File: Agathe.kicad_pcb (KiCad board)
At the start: 2 copper layers, 173 parts, among them SW1 SW_Push, U1 ATmega32U4-AU, Y1 Crystal_GND24_Small

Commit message: day 2 of work
MCU and USB routed
All switch routed between them
Todo: connect row and column to MCU
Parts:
- removed D44, D60, D62, D64, D67, D69, D71, D72: D_Small, Diode_SMD:D_SOD-123
- removed D76, D77: 3.6V, Diode_SMD:D_SOD-123
- removed MX44, MX60, MX67, MX69, MX71, MX72: MX-NoLED, MX_Only:MXOnly-1U-NoLED
- removed MX62: MX-NoLED, MX_Only:MXOnly-1.25U-NoLED
- removed MX64: MX-NoLED, MX_Only:MXOnly-2U-ReversedStabilizers-NoLED
- removed R7, R8: 75R, Resistor_SMD:R_0805_2012Metric
- removed R9: 1.5k, Resistor_SMD:R_0805_2012Metric
- added U2: PRTR5V0U2X, Package_TO_SOT_SMD:SOT-143, B.Cu at (180.2, 106.4)
- C1, C2, C3, C4, C5, C6, D10, D11, D12, D13, D14, D15, D16, D17, D18, D19, D2, D20, D21, D22, D23, D24, D25, D26, D27, D28, D29, D3, D30, D31, D32, D33, D34, D35, D36, D37, D38, D39, D4, D40, D41, D42, D43, D45, D46, D47, D48, D49, D5, D50, D51, D52, D53, D54, D55, D56, D57, D58, D59, D6, D61, D63, D65, D66, D68, D7, D70, D73, D74, D75, D8, D9, F1, R1, R2, R3, R4, R5, R6, Y1: moved to B.Cu
- C7: footprint Diode_SMD:D_SOD-123 -> Capacitor_SMD:C_0805_2012Metric; moved to B.Cu
- MX31: footprint MX_Only:MXOnly-1.25U-NoLED -> MX_Only:MXOnly-1.75U-NoLED
- MX43: footprint MX_Only:MXOnly-2.25U-NoLED -> MX_Only:MXOnly-2.25U-ReversedStabilizers-NoLED
- USB1: footprint Keebio-Parts:HRO-TYPE-C-31-M-12-Assembly -> Connector_USB:USB_C_Receptacle_HRO_TYPE-C-31-M-12
- moved D73 394.8 mm to (333.9, 181.0), turned to 90 degrees
- moved D59 381.3 mm to (353.0, 161.9), turned to 90 degrees
- moved D58 373.2 mm to (326.8, 161.9), turned to 90 degrees
- moved D45 332.8 mm to (371.7, 142.9), turned to 90 degrees
- moved D43 332.6 mm to (336.9, 142.9), turned to 90 degrees
- moved D70 328.8 mm to (262.8, 180.9), turned to 102 degrees
- moved D74 327.3 mm to (353.0, 181.0), turned to 90 degrees
- moved D75 324.1 mm to (372.0, 181.0), turned to 90 degrees
- moved D14 308.5 mm to (331.3, 104.8), turned to 90 degrees
- moved D68 299.2 mm to (225.5, 188.8), turned to 102 degrees
- moved D13 287.2 mm to (302.7, 104.8), turned to 90 degrees
- moved D30 273.7 mm to (367.6, 123.8), turned to 90 degrees
- moved D12 273.7 mm to (283.7, 104.8), turned to 90 degrees
- moved D56 270.2 mm to (281.6, 161.9), turned to 90 degrees
- moved D57 262.5 mm to (300.6, 161.9), turned to 90 degrees
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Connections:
- U1 pad 18: ROW0 -> COL13
- U1 pad 19: ROW1 -> COL12
- U1 pad 26: COL13 -> COL0
- U1 pad 27: COL12 -> COL1
- U1 pad 40: COL1 -> ROW1
- U1 pad 41: COL0 -> ROW0
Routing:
- net ROW4: track 0.00 -> 320.5 mm
- net GND: track 0.00 -> 274.8 mm, vias 0 -> 3
- net ROW0: track 0.00 -> 273.3 mm
- net ROW1: track 0.00 -> 268.1 mm
- net ROW2: track 0.00 -> 266.4 mm
- net ROW3: track 0.00 -> 257.3 mm
- net +5V: track 0.00 -> 151.3 mm, vias 0 -> 4
- net COL12: track 0.00 -> 99.8 mm
- net COL9: track 0.00 -> 87.3 mm
- net COL4: track 0.00 -> 86.8 mm
- net COL5: track 0.00 -> 86.8 mm
- net COL7: track 0.00 -> 86.0 mm
- net COL2: track 0.00 -> 85.7 mm
- net COL13: track 0.00 -> 85.2 mm
- net COL14: track 0.00 -> 81.9 mm
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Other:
- net class Default: trace_width 0.25 -> 0.254
- net class Power added: clearance 0.2, trace_width 0.381, via_dia 0.8, via_drill 0.4

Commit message: Route everything
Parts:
- moved D45 7.14 mm to (364.6, 144.0), turned to 0 degrees
- moved D75 7.14 mm to (365.0, 182.1), turned to 0 degrees
- moved SW1 3.71 mm to (194.4, 101.1)
- moved USB1 3.71 mm to (179.3, 93.1)
- moved F1 3.71 mm to (170.0, 99.8)
- moved R4 3.71 mm to (190.4, 105.8)
- moved R5 3.71 mm to (172.9, 99.5)
- moved R6 3.71 mm to (185.6, 99.5)
- moved U2 3.71 mm to (180.1, 102.7)
- moved D56 0.49 mm to (281.5, 161.4)
- moved D57 0.49 mm to (300.5, 161.4)
- moved D58 0.49 mm to (326.7, 161.4)
- moved D70 0.49 mm to (262.7, 180.4)
- moved MX40 0.49 mm to (258.2, 139.7)
- moved MX42 0.49 mm to (298.0, 139.7)
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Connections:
- U1 pad 1: COL2 -> Net-(U1-Pad1)
- U1 pad 10: Net-(U1-Pad10) -> COL9
- U1 pad 11: COL14 -> COL10
- U1 pad 12: COL9 -> COL11
- U1 pad 20: ROW2 -> ROW4
- U1 pad 22: ROW4 -> ROW2
- U1 pad 25: COL6 -> COL5
- U1 pad 26: COL0 -> COL4
- U1 pad 27: COL1 -> COL3
- U1 pad 28: COL11 -> COL2
- U1 pad 29: COL10 -> COL1
- U1 pad 30: COL5 -> COL0
- U1 pad 31: COL4 -> COL6
- U1 pad 32: COL3 -> COL14
- U1 pad 8: COL8 -> COL7
- U1 pad 9: COL7 -> COL8
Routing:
- net COL14: track 81.9 -> 334.4 mm, vias 0 -> 1
- net COL13: track 85.2 -> 303.2 mm, vias 0 -> 1
- net COL12: track 99.8 -> 291.4 mm, vias 0 -> 1
- net COL0: track 80.2 -> 256.9 mm, vias 0 -> 1
- net COL1: track 62.0 -> 219.0 mm, vias 0 -> 1
- net COL11: track 73.1 -> 220.3 mm, vias 0 -> 1
- net COL10: track 70.4 -> 207.0 mm, vias 0 -> 1
- net COL2: track 85.7 -> 218.2 mm, vias 0 -> 1
- net COL3: track 65.6 -> 177.1 mm, vias 0 -> 1
- net COL9: track 87.3 -> 186.7 mm, vias 0 -> 1
- net COL8: track 67.4 -> 162.6 mm, vias 0 -> 1
- net COL4: track 86.8 -> 178.5 mm, vias 0 -> 1
- net GND: track 274.8 -> 199.1 mm, vias 3 -> 2
- net ROW3: track 257.3 -> 332.9 mm, vias 0 -> 2
- net ROW0: track 273.3 -> 333.0 mm, vias 0 -> 4
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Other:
- board outline added: 338.8 x 114.1 mm

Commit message: change the enter footprint
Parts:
- MX43: footprint MX_Only:MXOnly-2.25U-ReversedStabilizers-NoLED -> MX_Only:MXOnly-2.25U-NoLED
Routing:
- net COL12: track 291.4 -> 293.9 mm
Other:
- board size 338.8 x 114.1 mm -> 338.8 x 114.8 mm

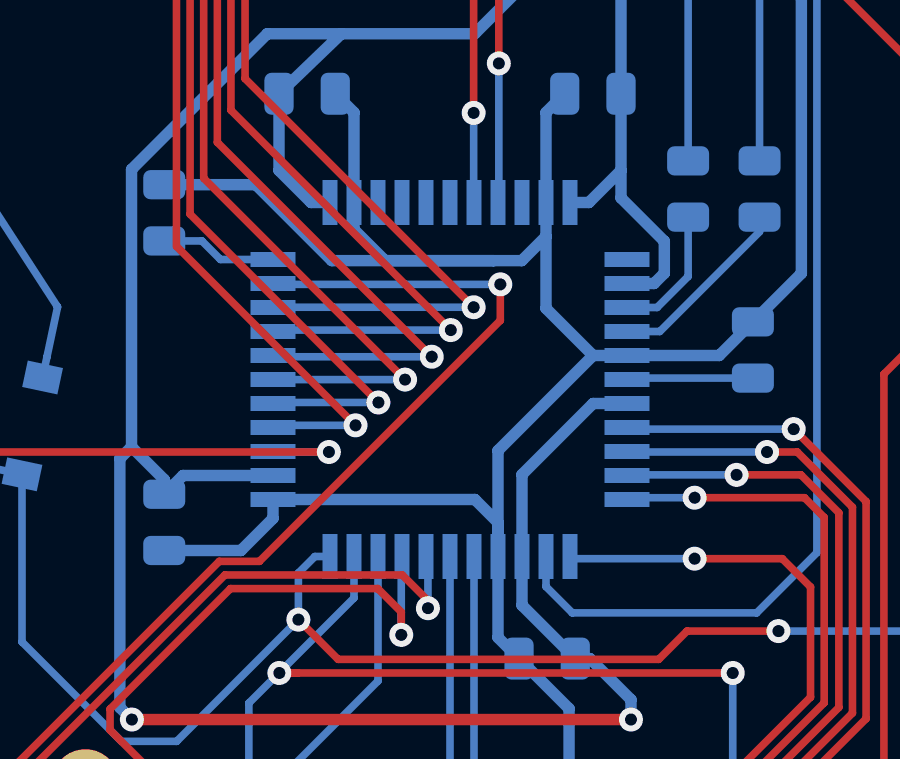
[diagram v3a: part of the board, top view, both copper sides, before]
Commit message: Add a proper usb-c
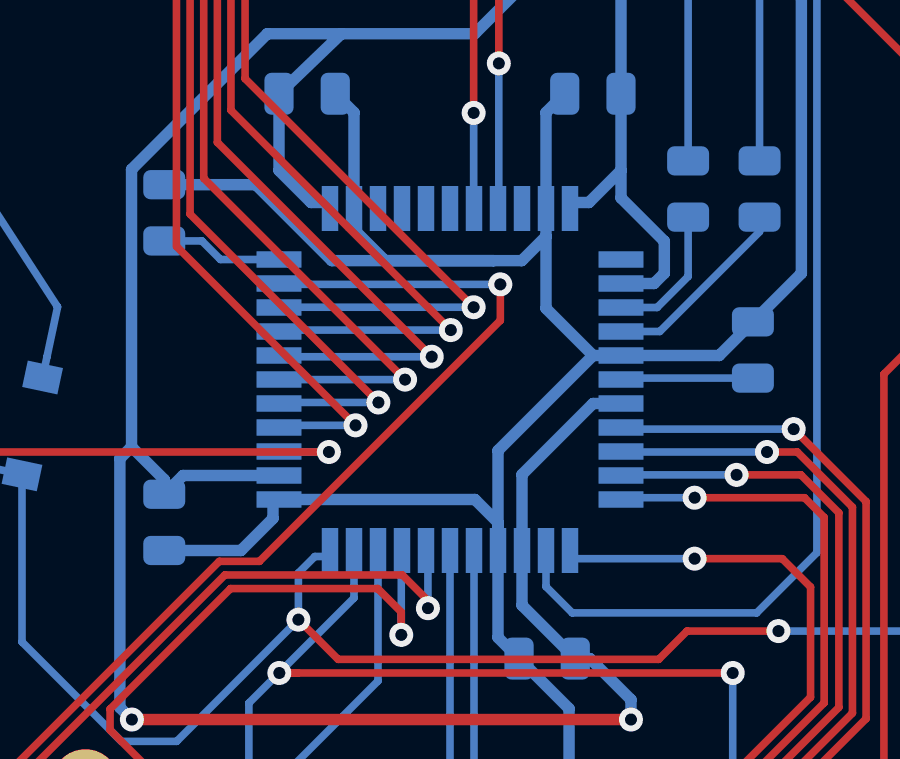
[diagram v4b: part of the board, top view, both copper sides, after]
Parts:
- U1: footprint Keebio-Parts:ATMEGA32U4-AU -> Package_QFP:TQFP-44_10x10mm_P0.8mm

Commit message: Add rotary encoder support
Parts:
- MX15, MX30, MX45: value MX-NoLED -> Rotary_Encoder_Switch; footprint MX_Only:MXOnly-1U-NoLED -> Rotary_Encoder:rotary_x_MX
- U1: footprint Package_QFP:TQFP-44_10x10mm_P0.8mm -> Keebio-Parts:ATMEGA32U4-AU
- moved D30 15.9 mm to (351.6, 123.3)
- moved D15 15.7 mm to (347.7, 104.3)
- moved D45 9.16 mm to (355.6, 142.4), turned to 90 degrees
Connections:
- U1 pad 38: Net-(U1-Pad38) -> COL7
- U1 pad 39: Net-(U1-Pad39) -> COL8
- U1 pad 8: COL7 -> ROTB
- U1 pad 9: COL8 -> ROTA
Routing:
- net ROTA: track 0.00 -> 255.0 mm, vias 0 -> 2
- net ROTB: track 0.00 -> 246.8 mm, vias 0 -> 2
- net GND: track 199.1 -> 264.9 mm
- net COL14: track 334.4 -> 380.8 mm
- net COL7: track 140.3 -> 162.7 mm
- net COL8: track 162.6 -> 181.1 mm
- net ROW1: track 317.4 -> 301.5 mm
- net ROW0: track 333.0 -> 317.3 mm
- net Net-(D45-Pad2): track 11.1 -> 19.9 mm
- net Net-(D30-Pad2): track 11.4 -> 19.8 mm
- net Net-(D15-Pad2): track 11.4 -> 19.6 mm
- net ROW2: track 319.5 -> 312.1 mm

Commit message: Add underglow
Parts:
- added LED1: WS2812B, LED_SMD:LED_WS2812B_PLCC4_5.0x5.0mm_P3.2mm, B.Cu at (193.5, 71.7)
- added LED10: WS2812B, LED_SMD:LED_WS2812B_PLCC4_5.0x5.0mm_P3.2mm, B.Cu at (302.7, 162.7)
- added LED11: WS2812B, LED_SMD:LED_WS2812B_PLCC4_5.0x5.0mm_P3.2mm, B.Cu at (362.8, 162.7)
- added LED12: WS2812B, LED_SMD:LED_WS2812B_PLCC4_5.0x5.0mm_P3.2mm, B.Cu at (375.2, 137.3)
- added LED13: WS2812B, LED_SMD:LED_WS2812B_PLCC4_5.0x5.0mm_P3.2mm, B.Cu at (375.2, 99.2)
- added LED14: WS2812B, LED_SMD:LED_WS2812B_PLCC4_5.0x5.0mm_P3.2mm, B.Cu at (347.4, 71.7)
- added LED15: WS2812B, LED_SMD:LED_WS2812B_PLCC4_5.0x5.0mm_P3.2mm, B.Cu at (290.3, 71.7)
- added LED16: WS2812B, LED_SMD:LED_WS2812B_PLCC4_5.0x5.0mm_P3.2mm, B.Cu at (235.9, 71.7)
- added LED2: WS2812B, LED_SMD:LED_WS2812B_PLCC4_5.0x5.0mm_P3.2mm, B.Cu at (139.7, 71.7)
- added LED3: WS2812B, LED_SMD:LED_WS2812B_PLCC4_5.0x5.0mm_P3.2mm, B.Cu at (70.9, 71.7)
- added LED4: WS2812B, LED_SMD:LED_WS2812B_PLCC4_5.0x5.0mm_P3.2mm, B.Cu at (43.3, 99.2)
- added LED5: WS2812B, LED_SMD:LED_WS2812B_PLCC4_5.0x5.0mm_P3.2mm, B.Cu at (43.3, 137.3)
- added LED6: WS2812B, LED_SMD:LED_WS2812B_PLCC4_5.0x5.0mm_P3.2mm, B.Cu at (76.8, 162.7)
- added LED7: WS2812B, LED_SMD:LED_WS2812B_PLCC4_5.0x5.0mm_P3.2mm, B.Cu at (139.7, 170.7)
- added LED8: WS2812B, LED_SMD:LED_WS2812B_PLCC4_5.0x5.0mm_P3.2mm, B.Cu at (188.4, 179.4)
- added LED9: WS2812B, LED_SMD:LED_WS2812B_PLCC4_5.0x5.0mm_P3.2mm, B.Cu at (242.3, 169.3)
- moved D66 23.0 mm to (178.8, 174.1)
- moved D63 23.0 mm to (118.2, 161.3)
- moved D65 23.0 mm to (148.5, 167.7)
- moved D73 23.0 mm to (338.9, 158.1)
- moved D74 23.0 mm to (357.9, 158.1)
- moved D61 23.0 mm to (62.0, 158.1)
- moved D70 23.0 mm to (267.7, 158.0)
- moved D75 23.0 mm to (370.0, 159.7)
- moved D48 22.0 mm to (119.9, 143.2)
- moved MX7 22.0 mm to (175.9, 93.9)
- moved D41 22.0 mm to (291.9, 121.0)
- moved MX36 22.0 mm to (163.3, 130.2)
- moved MX39 22.0 mm to (244.6, 122.2)
- moved D3 22.0 mm to (107.3, 82.9)
- moved D14 22.0 mm to (336.2, 82.9)
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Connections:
- U1 pad 30: COL0 -> LED
- U1 pad 31: COL6 -> COL0
- U1 pad 36: Net-(U1-Pad36) -> COL6
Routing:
- net +5V: track 158.4 -> 985.7 mm, vias 4 -> 5
- net LED: track 0.00 -> 105.2 mm, vias 0 -> 4
- net Net-(LED2-Pad2): track 0.00 -> 65.6 mm
- net Net-(LED6-Pad2): track 0.00 -> 59.3 mm
- net Net-(LED10-Pad4): track 0.00 -> 58.1 mm
- net Net-(LED10-Pad2): track 0.00 -> 57.0 mm
- net Net-(LED13-Pad2): track 0.00 -> 53.7 mm
- net Net-(LED14-Pad2): track 0.00 -> 53.6 mm
- net Net-(LED8-Pad2): track 0.00 -> 52.5 mm
- net Net-(LED1-Pad2): track 0.00 -> 51.3 mm
- net Net-(LED15-Pad2): track 0.00 -> 50.8 mm
- net Net-(LED5-Pad2): track 0.00 -> 49.5 mm
- net Net-(LED3-Pad2): track 0.00 -> 47.1 mm
- net Net-(LED7-Pad2): track 0.00 -> 46.3 mm
- net Net-(LED11-Pad2): track 0.00 -> 36.4 mm
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- added copper zone on B.Cu, net GND
- added copper zone on F.Cu, net GND

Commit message: Update footprints for switch
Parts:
- added G***: LOGO, cc:cc, F.Cu at (81.8, 156.4)
- MX1, MX10, MX11, MX12, MX13, MX17, MX18, MX19, MX2, MX20, MX21, MX22, MX23, MX24, MX25, MX26, MX27, MX28, MX3, MX32, MX33, MX34, MX35, MX36, MX37, MX38, MX39, MX4, MX40, MX41, MX42, MX47, MX48, MX49, MX5, MX50, MX51, MX52, MX53, MX54, MX55, MX56, MX57, MX59, MX6, MX7, MX73, MX74, MX75, MX8, MX9: footprint MX_Only:MXOnly-1U-NoLED -> parts:mx_1u
- MX14: footprint MX_Only:MXOnly-2U-NoLED -> parts:mx_2u
- MX16, MX29, MX61: footprint MX_Only:MXOnly-1.5U-NoLED -> parts:mx_15u
- MX31, MX58: footprint MX_Only:MXOnly-1.75U-NoLED -> parts:mx_175u
- MX43, MX46: footprint MX_Only:MXOnly-2.25U-NoLED -> parts:mx_225u
- MX63, MX66, MX70: footprint MX_Only:MXOnly-1.25U-NoLED -> parts:mx_125u
- MX65: footprint MX_Only:MXOnly-2U-ReversedStabilizers-NoLED -> parts:mx_2ureverse
- MX68: footprint MX_Only:MXOnly-2.75U-ReversedStabilizers-NoLED -> parts:mx_275u_reverse

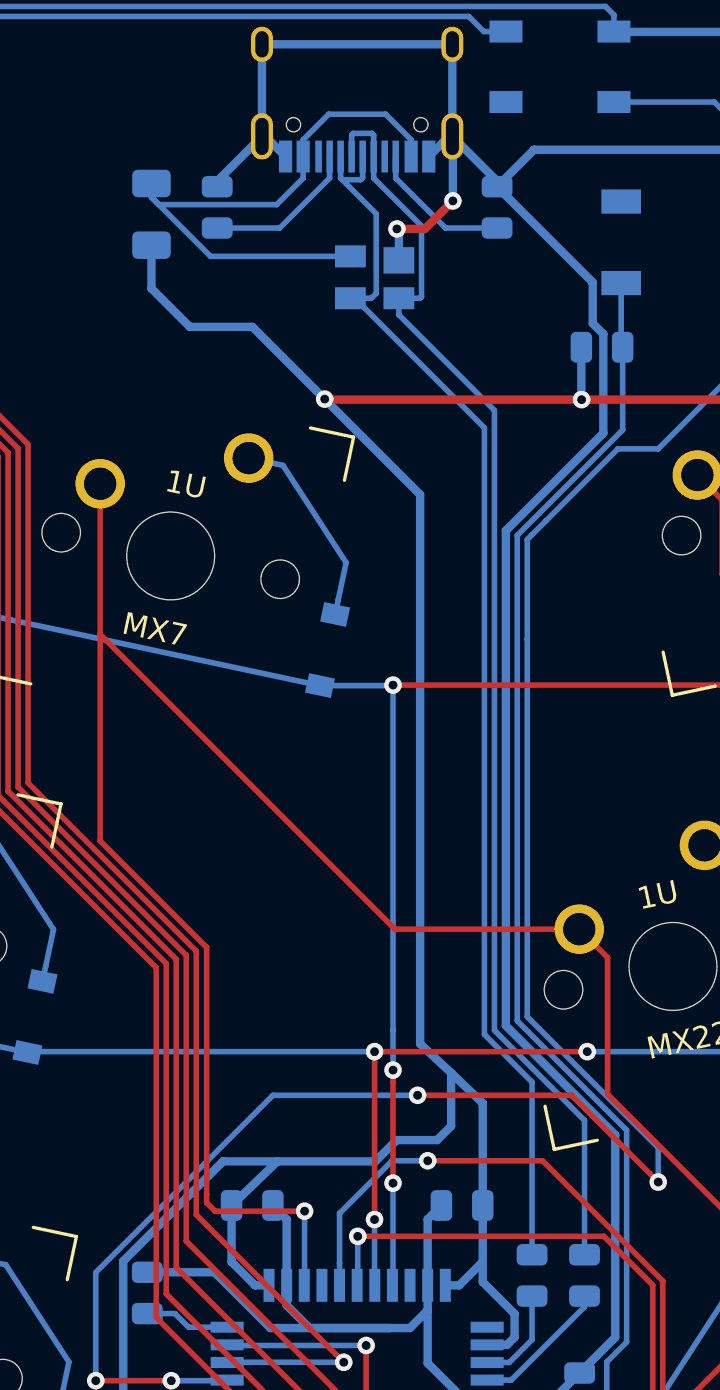
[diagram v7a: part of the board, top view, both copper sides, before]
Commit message: Rerouting around USB-C connector
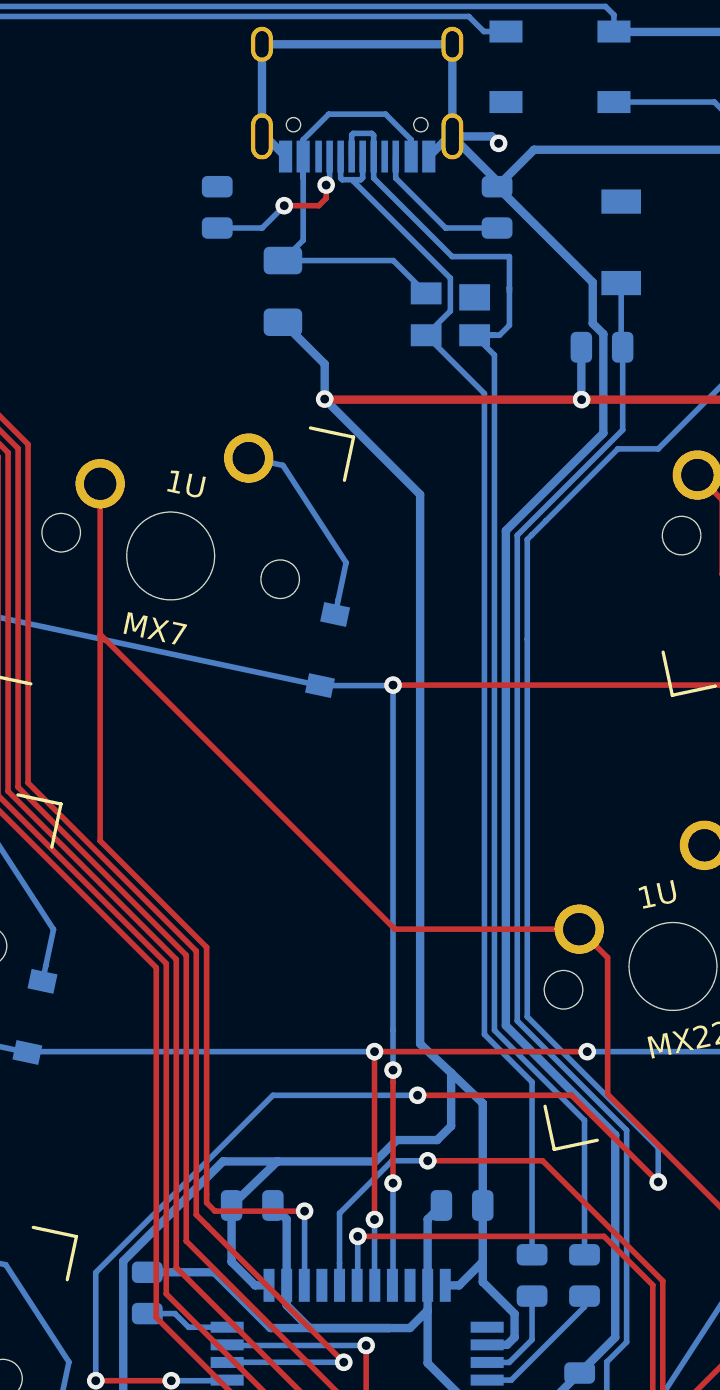
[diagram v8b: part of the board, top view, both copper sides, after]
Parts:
- moved F1 6.91 mm to (181.0, 81.9)
- moved U2 3.83 mm to (188.6, 82.9)
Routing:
- net GND: track 264.9 -> 256.8 mm, vias 7 -> 6
- net +5V: track 985.7 -> 978.1 mm
- net VCC: track 26.7 -> 20.6 mm
- net D+: track 58.3 -> 61.4 mm
- net D-: track 57.1 -> 56.1 mm
- net Net-(R5-Pad2): track 7.02 -> 7.09 mm, vias 0 -> 2
